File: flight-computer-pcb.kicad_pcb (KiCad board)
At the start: 4 copper layers, 140 x 80 mm, 7 parts, among them U1 Teensy4.1, U10 U3V16F9, U2 BMP390, U3 BNO055, U7 U3V70F6, U8 S7V8F3, U9 S13V10F5

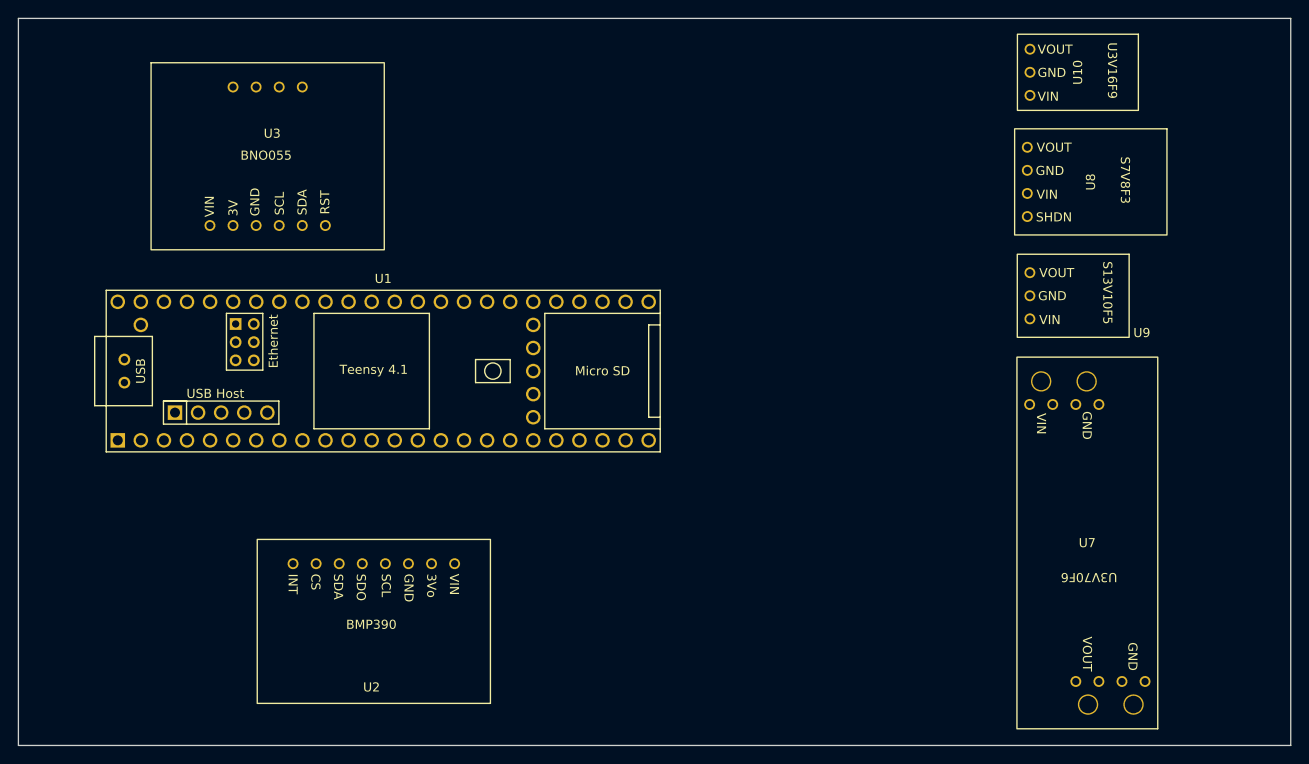
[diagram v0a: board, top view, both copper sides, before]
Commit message: feat: add M4 mounting holes
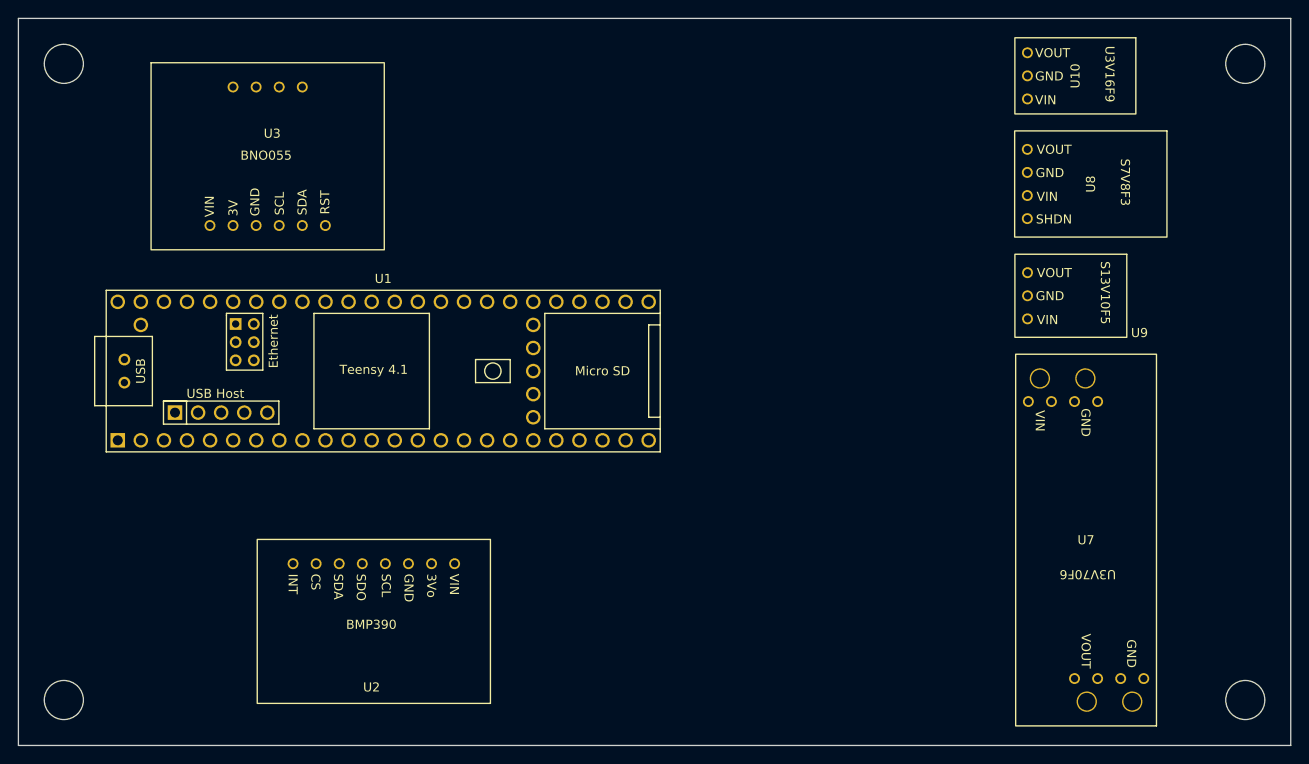
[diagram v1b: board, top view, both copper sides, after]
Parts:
- added REF**: MountingHole_4.3mm_M4, MountingHole:MountingHole_4.3mm_M4, F.Cu at (85.0, 65.0)
- added REF**: MountingHole_4.3mm_M4, MountingHole:MountingHole_4.3mm_M4, F.Cu at (215.0, 65.0)
- added REF**: MountingHole_4.3mm_M4, MountingHole:MountingHole_4.3mm_M4, F.Cu at (85.0, 135.0)
- added REF**: MountingHole_4.3mm_M4, MountingHole:MountingHole_4.3mm_M4, F.Cu at (215.0, 135.0)
- moved U10 0.48 mm to (196.3, 66.3)
- moved U7 0.35 mm to (197.5, 117.4)
- moved U9 0.26 mm to (195.8, 90.5)
- moved U8 0.23 mm to (198.0, 78.2)

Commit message: feat: add connector footprints to J1, J2 and J3
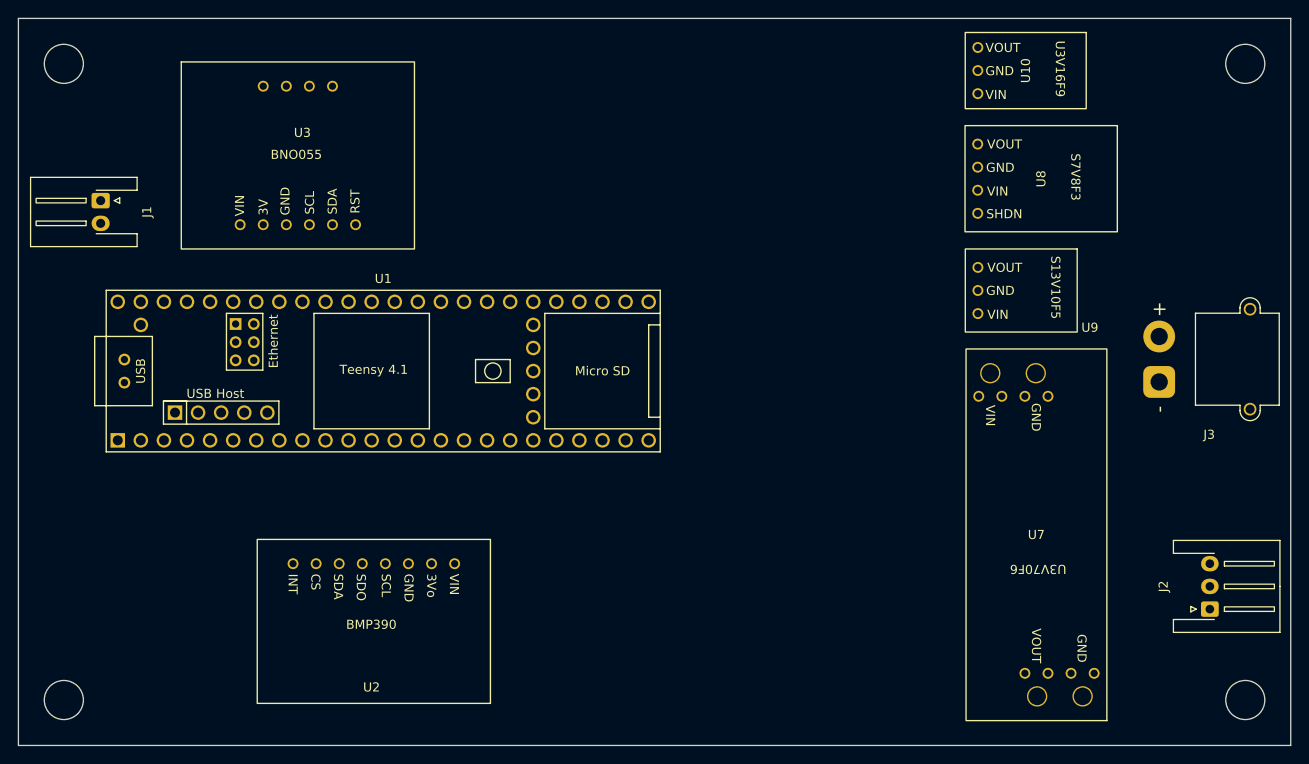
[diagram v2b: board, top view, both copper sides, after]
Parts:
- added J1: Conn_02x01, Connector_JST:JST_XH_S2B-XH-A-1_1x02_P2.50mm_Horizontal, F.Cu at (89.0, 80.0)
- added J2: Conn_01x03, Connector_JST:JST_XH_S3B-XH-A-1_1x03_P2.50mm_Horizontal, F.Cu at (211.1, 125.0)
- added J3: Conn_02x01, Connector_AMASS:AMASS_XT30PW-M_1x02_P2.50mm_Horizontal, F.Cu at (205.5, 100.0)
- moved U10 5.49 mm to (190.8, 65.7)
- moved U8 5.49 mm to (192.5, 77.6)
- moved U9 5.49 mm to (190.3, 89.9)
- moved U7 5.49 mm to (192.0, 116.8)
- moved U3 3.32 mm to (110.8, 75.1)
